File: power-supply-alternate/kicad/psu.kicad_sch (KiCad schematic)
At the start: 16 parts, among them J3 SSQ-103-03-G-D, U1 MAX889TESA+, U3 TPS72301DBVR, U5 TPS79333DBVR

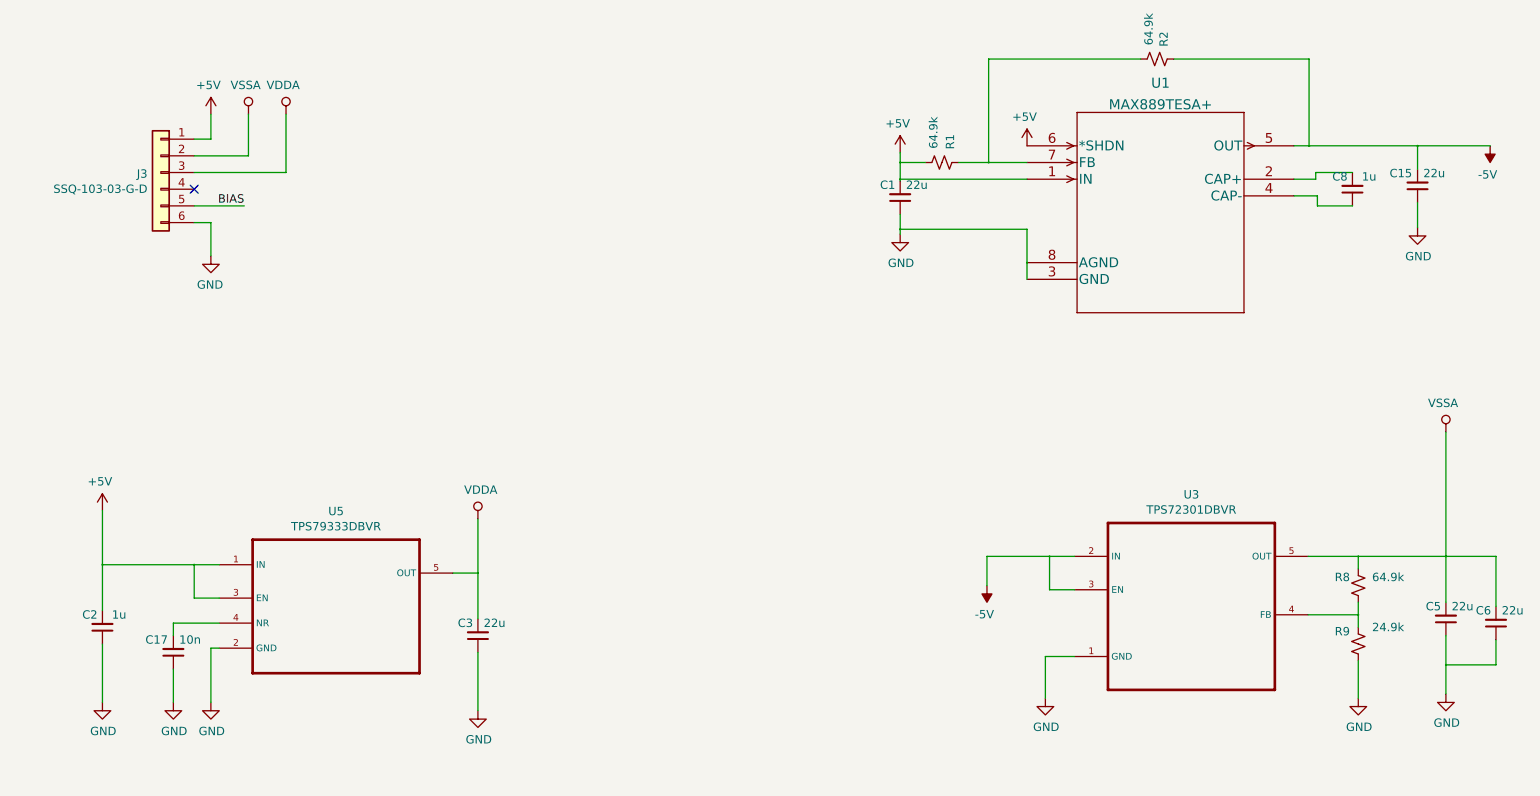
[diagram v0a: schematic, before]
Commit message: Check in (tested) alternative psu
Can use easier to get parts for the charge pump and positive regulator.

Specs are actually better than the original design but the difference is insignificant.  We bumped the negative voltage rail up a little (-4.6V) due to better parts.

Can use the existing TPS79333 (which is hard to find) or the tps7a20 which has better specs and is pin compatible.  Can optionally use the 4.2 or 4.5v version as well to extend dynamic range, although this won't make a difference with the current bias generator and s14420 due to current limits.  Maybe help if used with other SiPMs.
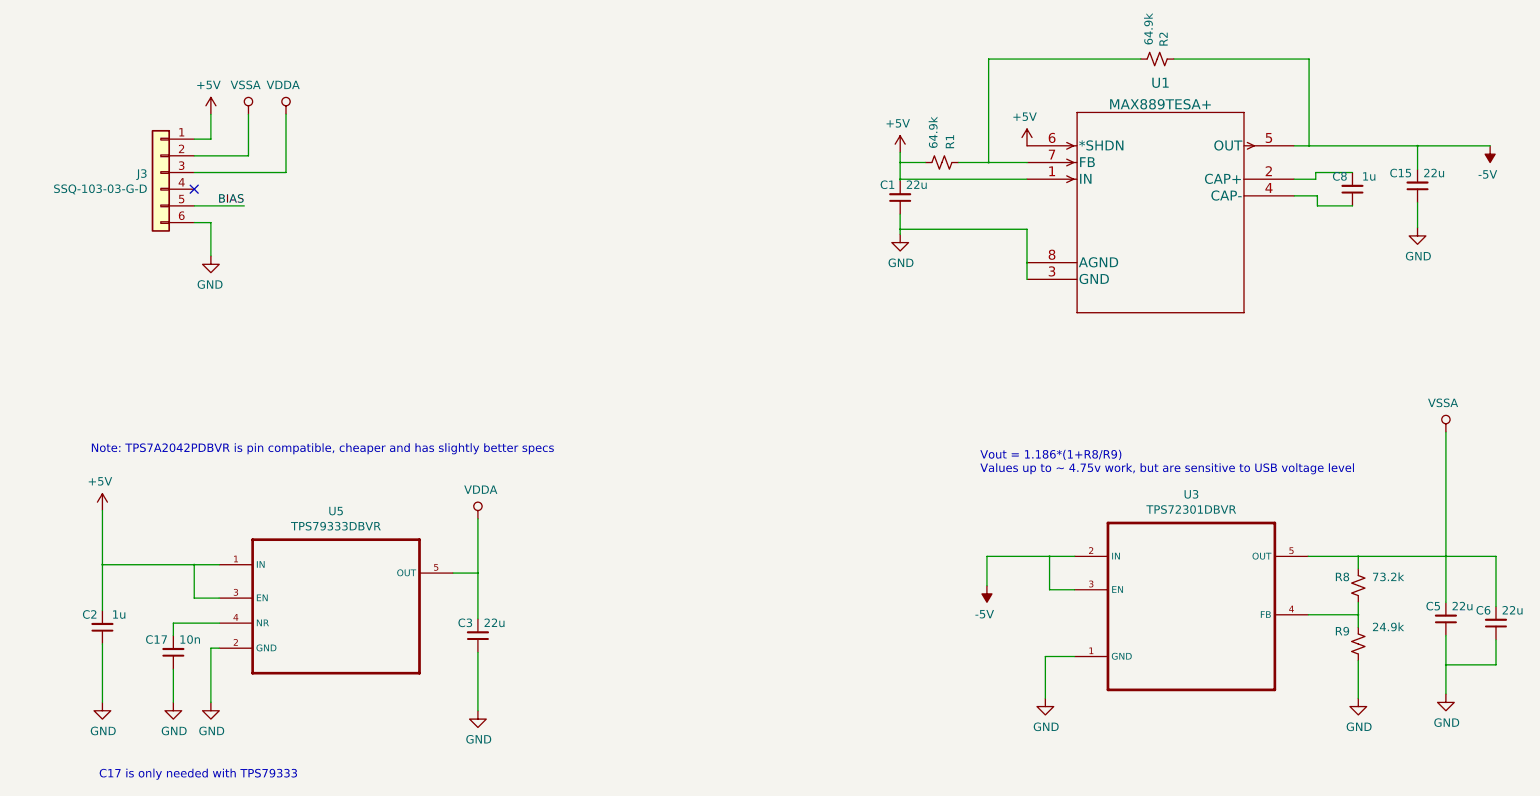
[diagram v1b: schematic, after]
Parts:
- R8: value 64.9k -> 73.2k
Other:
- note added: "C17 is only needed with TPS79333"
- note added: "Note: TPS7A2042PDBVR is pin compatible, cheaper and has slightly better specs"
- note added: "Vout = 1.186*(1+R8/R9) Values up to ~ 4.75v work, but are sensitive to USB voltage level"
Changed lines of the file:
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@@
     (stroke (width 0) (type solid) (color 0 0 0 0))
+  )
+  (text "Note: TPS7A2042PDBVR is pin compatible, cheaper and has slightly better specs"
+    (at 57.912 96.266 0)
+    (effects (font (size 1.27 1.27)) (justify left bottom))
+  )
+  (text "C17 is only needed with TPS79333" (at 59.182 145.796 0)
+    (effects (font (size 1.27 1.27)) (justify left bottom))
+  )
+  (text "Vout = 1.186*(1+R8/R9)\nValues up to ~ 4.75v work, but are sensitive to USB voltage level"
+    (at 193.294 99.314 0)
+    (effects (font (size 1.27 1.27)) (justify left bottom))
   )
   (label "BIAS" (at 81.28 58.42 180)
@@
       (effects (font (size 1.27 1.27)) (justify left))
     )
-    (property "Value" "64.9k" (id 1) (at 257.81 114.935 0)
+    (property "Value" "73.2k" (id 1) (at 257.81 114.935 0)
       (effects (font (size 1.27 1.27)) (justify left))
     )
@@
     )
     (path "/00000000-0000-0000-0000-00005b21abec"
-      (reference "R8") (unit 1) (value "64.9k") (footprint "footprints:R_0603_1608Metric")
+      (reference "R8") (unit 1) (value "73.2k") (footprint "footprints:R_0603_1608Metric")
     )
     (path "/00000000-0000-0000-0000-00005b21b93f"
